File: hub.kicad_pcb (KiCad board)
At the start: 2 copper layers, 0 parts

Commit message: chore(revb): checkpoint current KiCad files before TI revision
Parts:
- added T1: 750313638, isolator-lib:WE_750313638, F.Cu at (166.2, 113.7)

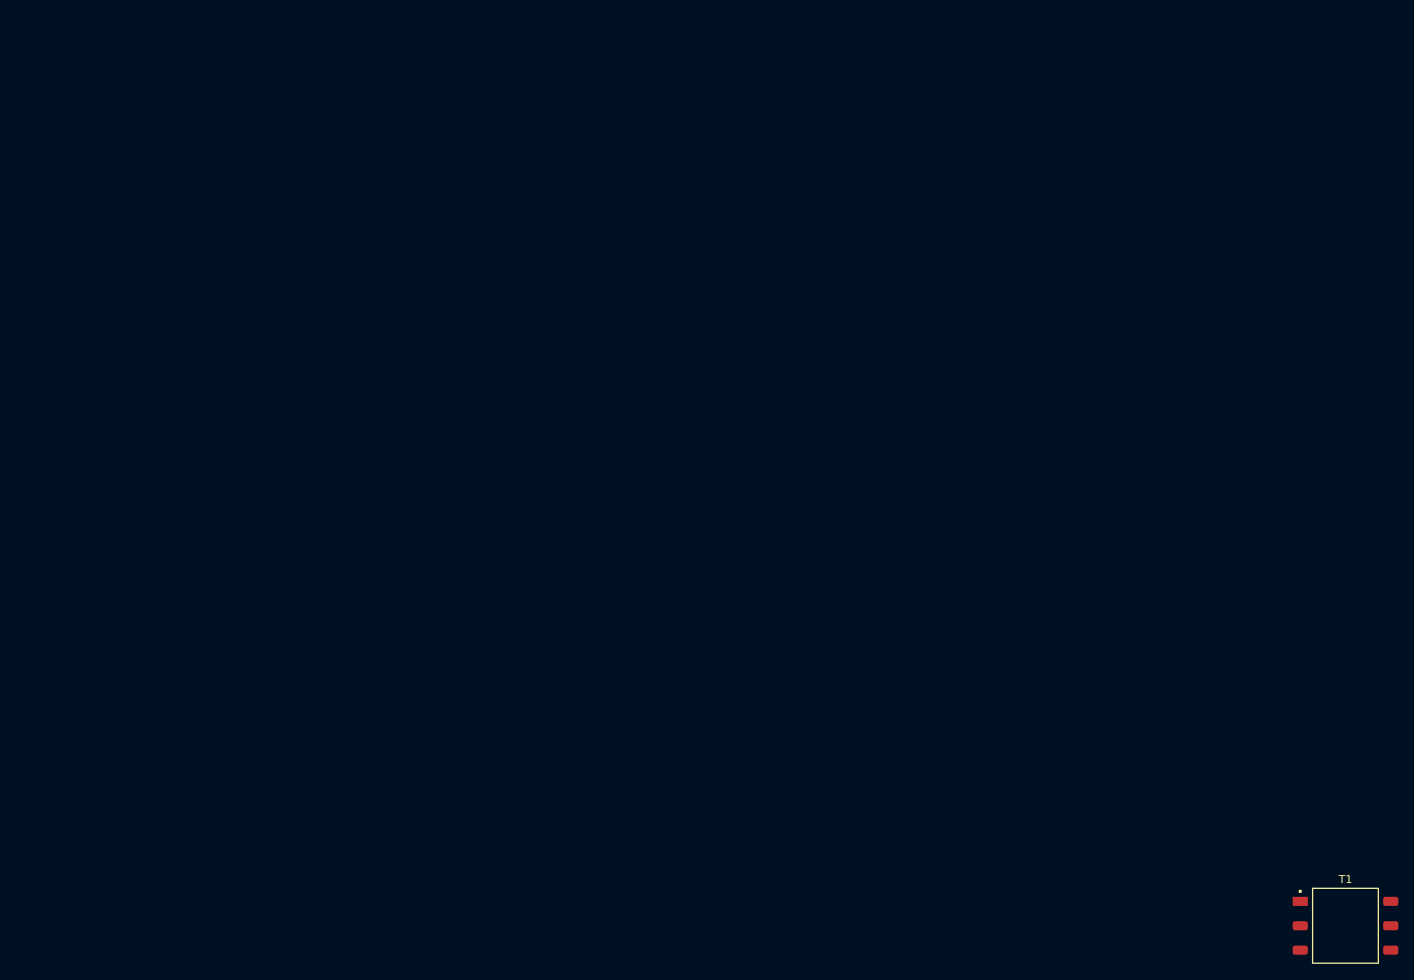
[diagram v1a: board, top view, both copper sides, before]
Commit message: feat(revc): place synchronized unrouted board and correct bus startup
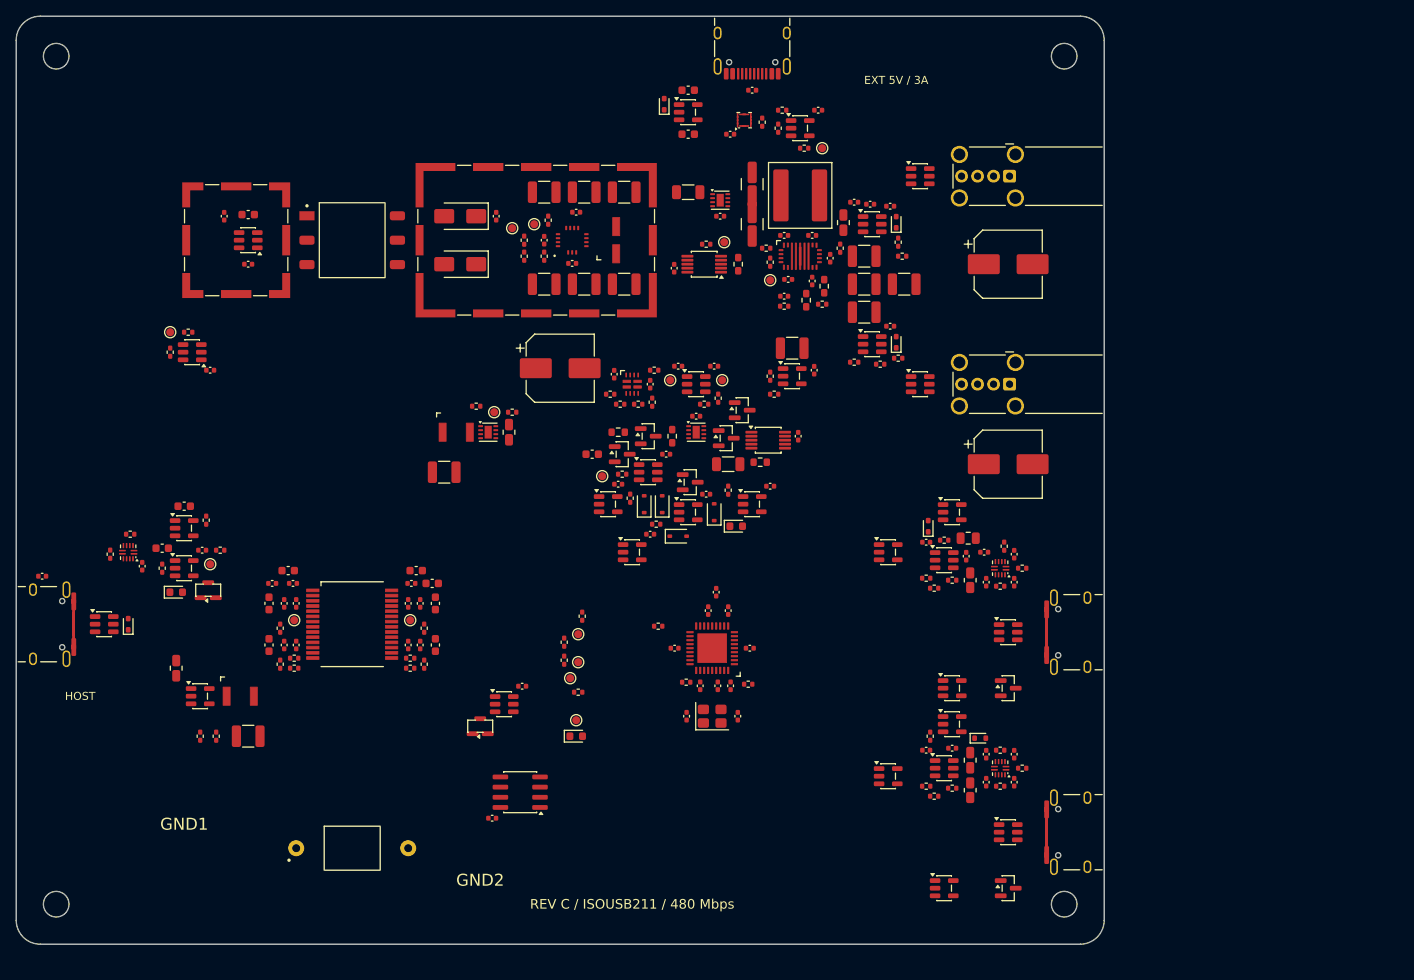
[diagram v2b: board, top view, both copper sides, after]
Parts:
- added C1: 100nF, hub-lib:C_0402_1005Metric, F.Cu at (3.25, 70.0)
- added C10: 100nF, hub-lib:C_0402_1005Metric, F.Cu at (26.0, 25.0)
- added C100: 100nF, hub-lib:C_0402_1005Metric, F.Cu at (121.2, 70.8)
- added C101: 100nF, hub-lib:C_0402_1005Metric, F.Cu at (124.8, 67.2)
- added C102: 100nF, hub-lib:C_0402_1005Metric, F.Cu at (124.8, 70.8)
- added C103: 100nF, hub-lib:C_0402_1005Metric, F.Cu at (121.2, 92.2)
- added C104: 100nF, hub-lib:C_0402_1005Metric, F.Cu at (121.2, 95.8)
- added C105: 100nF, hub-lib:C_0402_1005Metric, F.Cu at (124.8, 92.2)
- added C106: 100nF, hub-lib:C_0402_1005Metric, F.Cu at (124.8, 95.8)
- added C107: 100nF, hub-lib:C_0402_1005Metric, F.Cu at (86.2, 59.8)
- added C108: 100nF, hub-lib:C_0402_1005Metric, F.Cu at (75.2, 58.5)
- added C109: 100nF, hub-lib:C_0402_1005Metric, F.Cu at (79.2, 64.8)
- added C11: 4.7uF, hub-lib:C_0603_1608Metric, F.Cu at (29.0, 24.8)
- added C110: 100nF, hub-lib:C_0402_1005Metric, F.Cu at (82.2, 31.5)
- added C112: 100nF, hub-lib:C_0402_1005Metric, F.Cu at (97.8, 52.5)
- added C113: 4.7uF, hub-lib:C_0805_2012Metric, F.Cu at (20.0, 81.5)
- added C114: 22uF, hub-lib:C_1210_3225Metric, F.Cu at (29.0, 90.0)
- added C115: 22nF, hub-lib:C_0402_1005Metric, F.Cu at (85.0, 50.0)
- added C116: 22uF, hub-lib:C_1210_3225Metric, F.Cu at (97.0, 41.5)
- added C117: 100nF, hub-lib:C_0402_1005Metric, F.Cu at (99.8, 44.2)
- added C12: 100nF, hub-lib:C_0402_1005Metric, F.Cu at (29.0, 31.0)
- added C13: 22uF, hub-lib:C_1210_3225Metric, F.Cu at (66.0, 33.5)
- added C14: 100nF, hub-lib:C_0402_1005Metric, F.Cu at (60.0, 25.0)
- added C15: 22uF, hub-lib:C_1210_3225Metric, F.Cu at (71.0, 33.5)
- added C16: 22uF, hub-lib:C_1210_3225Metric, F.Cu at (76.0, 33.5)
- added C17: 100nF, hub-lib:C_0402_1005Metric, F.Cu at (69.5, 30.9)
- added C18: 22uF, hub-lib:C_1210_3225Metric, F.Cu at (66.0, 22.0)
- added C19: 22uF, hub-lib:C_1210_3225Metric, F.Cu at (71.0, 22.0)
- added C2: 1uF, hub-lib:C_0603_1608Metric, F.Cu at (21.0, 61.2)
- added C20: 22uF, hub-lib:C_1210_3225Metric, F.Cu at (76.0, 22.0)
- added C21: 100nF, hub-lib:C_0402_1005Metric, F.Cu at (70.0, 24.5)
- added C22: 100nF, hub-lib:C_0402_1005Metric, F.Cu at (66.0, 28.0)
- added C23: 100nF, hub-lib:C_0402_1005Metric, F.Cu at (92.0, 9.25)
- added C24: 1uF, hub-lib:C_0603_1608Metric, F.Cu at (84.0, 9.25)
- added C25: 100nF, hub-lib:C_0402_1005Metric, F.Cu at (89.2, 14.8)
- added C26: 100nF, hub-lib:C_0402_1005Metric, F.Cu at (100.2, 11.8)
- added C27: 100nF, hub-lib:C_0402_1005Metric, F.Cu at (74.8, 44.8)
- added C28: 1uF, hub-lib:C_0603_1608Metric, F.Cu at (50.0, 69.3)
- added C29: 100nF, hub-lib:C_0402_1005Metric, F.Cu at (49.4, 70.9)
- added C3: 1uF, hub-lib:C_0603_1608Metric, F.Cu at (34.0, 69.3)
- added C30: 10uF, hub-lib:C_0805_2012Metric, F.Cu at (61.6, 52.0)
- added C31: 22uF, hub-lib:C_1210_3225Metric, F.Cu at (53.5, 57.0)
- added C32: 27pF, hub-lib:C_0402_1005Metric, F.Cu at (83.8, 87.5)
- added C33: 27pF, hub-lib:C_0402_1005Metric, F.Cu at (90.2, 87.5)
- added C34: 100nF, hub-lib:C_0402_1005Metric, F.Cu at (87.5, 72.0)
- added C35: 100nF, hub-lib:C_0402_1005Metric, F.Cu at (91.7, 79.0)
- added C36: 100nF, hub-lib:C_0402_1005Metric, F.Cu at (89.0, 74.3)
- added C37: 100nF, hub-lib:C_0402_1005Metric, F.Cu at (86.5, 74.3)
- added C38: 100nF, hub-lib:C_0402_1005Metric, F.Cu at (82.3, 79.0)
- added C39: 100nF, hub-lib:C_0402_1005Metric, F.Cu at (85.5, 83.7)
- added C4: 100nF, hub-lib:C_0402_1005Metric, F.Cu at (34.6, 70.9)
- added C40: 100nF, hub-lib:C_0402_1005Metric, F.Cu at (89.3, 83.7)
- added C41: 4.7uF, hub-lib:C_0603_1608Metric, F.Cu at (72.0, 54.8)
- added C42: 100nF, hub-lib:C_0402_1005Metric, F.Cu at (63.2, 83.8)
- added C43: 100nF, hub-lib:C_0402_1005Metric, F.Cu at (104.8, 23.2)
- added C44: 220uF, hub-lib:CP_Elec_8x6.2, F.Cu at (124.0, 31.0)
- added C45: 100nF, hub-lib:C_0402_1005Metric, F.Cu at (109.2, 23.8)
- added C46: 100nF, hub-lib:C_0402_1005Metric, F.Cu at (106.8, 23.5)
- added C47: 220uF, hub-lib:CP_Elec_8x6.2, F.Cu at (124.0, 56.0)
- added C48: 100nF, hub-lib:C_0402_1005Metric, F.Cu at (109.2, 38.8)
- added C49: 100nF, hub-lib:C_0402_1005Metric, F.Cu at (113.8, 65.8)
- added C50: 10uF, hub-lib:C_0805_2012Metric, F.Cu at (119.0, 65.2)
- added C51: 100nF, hub-lib:C_0402_1005Metric, F.Cu at (118.8, 67.5)
- added C55: 100nF, hub-lib:C_0402_1005Metric, F.Cu at (113.8, 91.8)
- added C56: 10uF, hub-lib:C_0805_2012Metric, F.Cu at (119.2, 93.0)
- added C57: 100nF, hub-lib:C_0402_1005Metric, F.Cu at (117.0, 91.5)
- added C59: 100nF, hub-lib:C_0402_1005Metric, F.Cu at (87.7, 83.7)
- added C61: 1uF, hub-lib:C_0603_1608Metric, F.Cu at (18.2, 66.5)
- added C62: 100nF, hub-lib:C_0402_1005Metric, F.Cu at (24.2, 44.2)
- added C63: 100nF, hub-lib:C_0402_1005Metric, F.Cu at (32.0, 70.9)
- added C64: 1uF, hub-lib:C_0603_1608Metric, F.Cu at (52.0, 70.9)
- added C65: 4.7uF, hub-lib:C_0603_1608Metric, F.Cu at (31.6, 73.4)
- added C66: 100nF, hub-lib:C_0402_1005Metric, F.Cu at (33.5, 73.4)
- added C67: 10nF, hub-lib:C_0402_1005Metric, F.Cu at (35.0, 73.4)
- added C68: 4.7uF, hub-lib:C_0603_1608Metric, F.Cu at (31.6, 78.6)
- added C69: 100nF, hub-lib:C_0402_1005Metric, F.Cu at (33.5, 78.6)
- added C7: 100nF, hub-lib:C_0402_1005Metric, F.Cu at (15.8, 68.8)
- added C70: 10nF, hub-lib:C_0402_1005Metric, F.Cu at (35.0, 78.6)
- added C71: 4.7uF, hub-lib:C_0603_1608Metric, F.Cu at (52.4, 73.4)
- added C72: 100nF, hub-lib:C_0402_1005Metric, F.Cu at (50.5, 73.4)
- added C73: 10nF, hub-lib:C_0402_1005Metric, F.Cu at (49.0, 73.4)
- added C74: 4.7uF, hub-lib:C_0603_1608Metric, F.Cu at (52.4, 78.6)
- added C75: 100nF, hub-lib:C_0402_1005Metric, F.Cu at (50.5, 78.6)
- added C76: 10nF, hub-lib:C_0402_1005Metric, F.Cu at (49.0, 78.6)
- added C77: 1uF, hub-lib:C_0603_1608Metric, F.Cu at (84.0, 14.8)
- added C78: 10nF, hub-lib:C_0402_1005Metric, F.Cu at (88.0, 25.0)
- added C79: 22uF, hub-lib:C_1210_3225Metric, F.Cu at (92.0, 21.0)
- added C8: 100nF, hub-lib:C_0402_1005Metric, F.Cu at (23.2, 66.8)
- added C80: 22uF, hub-lib:C_1210_3225Metric, F.Cu at (92.0, 26.0)
- added C81: 100nF, hub-lib:C_0402_1005Metric, F.Cu at (96.5, 32.9)
- added C82: 100nF, hub-lib:C_0402_1005Metric, F.Cu at (96.0, 27.4)
- added C83: 100nF, hub-lib:C_0402_1005Metric, F.Cu at (99.5, 27.4)
- added C84: 10uF, hub-lib:C_0805_2012Metric, F.Cu at (103.4, 25.8)
- added C85: 22uF, hub-lib:C_1210_3225Metric, F.Cu at (106.0, 30.0)
- added C86: 22uF, hub-lib:C_1210_3225Metric, F.Cu at (106.0, 33.5)
- added C87: 22uF, hub-lib:C_1210_3225Metric, F.Cu at (106.0, 37.0)
- added C88: 22uF, hub-lib:C_1210_3225Metric, F.Cu at (111.0, 33.5)
- added C89: 100nF, hub-lib:C_0402_1005Metric, F.Cu at (99.5, 33.1)
- added C90: 220nF, hub-lib:C_0402_1005Metric, F.Cu at (96.0, 35.0)
- added C91: 100pF, hub-lib:C_0402_1005Metric, F.Cu at (101.8, 30.2)
- added C92: 220uF, hub-lib:CP_Elec_8x6.2, F.Cu at (68.0, 44.0)
- added C93: 100nF, hub-lib:C_0402_1005Metric, F.Cu at (79.2, 46.0)
- added C94: 100nF, hub-lib:C_0402_1005Metric, F.Cu at (81.2, 54.8)
- added C95: 100nF, hub-lib:C_0402_1005Metric, F.Cu at (94.2, 58.8)
- added C96: 100nF, hub-lib:C_0402_1005Metric, F.Cu at (82.8, 43.8)
- added C97: 100nF, hub-lib:C_0402_1005Metric, F.Cu at (87.2, 43.8)
- added C98: 100nF, hub-lib:C_0402_1005Metric, F.Cu at (59.5, 100.2)
- added C99: 100nF, hub-lib:C_0402_1005Metric, F.Cu at (121.0, 67.0)
- added CY1: 1nF Y1, hub-lib:C_Disc_D7.0mm_W5.5mm_P14.00mm, F.Cu at (35.0, 104.0)
- added D1: T6V0S5A-7, hub-lib:D_SOD-523, F.Cu at (14.0, 76.0)
- added D10: T6V0S5A-7, hub-lib:D_SOD-523, F.Cu at (114.0, 63.8)
- added D13: T6V0S5A-7, hub-lib:D_SOD-523, F.Cu at (120.5, 90.2)
- added D14: BAT54WS, hub-lib:D_SOD-323, F.Cu at (80.8, 61.0)
- added D15: BAT54WS, hub-lib:D_SOD-323, F.Cu at (82.8, 65.0)
- added D16: BAT54WS, hub-lib:D_SOD-323, F.Cu at (87.2, 62.0)
- added D17: BAT54WS, hub-lib:D_SOD-323, F.Cu at (78.5, 61.0)
- added D2: GREEN, hub-lib:LED_0603_1608Metric, F.Cu at (20.0, 72.0)
- added D20: BAT54C, hub-lib:SOT-23, F.Cu at (84.2, 58.2)
- added D21: BAT54C, hub-lib:SOT-23, F.Cu at (90.8, 49.2)
- added D22: BAT54C, hub-lib:SOT-23, F.Cu at (75.8, 54.8)
- added D23: BAT54C, hub-lib:SOT-23, F.Cu at (79.0, 52.5)
- added D3: SS34, hub-lib:D_SMA, F.Cu at (55.5, 31.0)
- added D4: SS34, hub-lib:D_SMA, F.Cu at (55.5, 25.0)
- added D5: T6V0S5A-7, hub-lib:D_SOD-523, F.Cu at (81.0, 11.0)
- added D6: GREEN, hub-lib:LED_0603_1608Metric, F.Cu at (90.0, 63.8)
- added D7: GREEN, hub-lib:LED_0603_1608Metric, F.Cu at (70.0, 90.0)
- added D8: T6V0S5A-7, hub-lib:D_SOD-523, F.Cu at (110.0, 25.8)
- added D9: T6V0S5A-7, hub-lib:D_SOD-523, F.Cu at (110.0, 40.8)
- added H1: M3 NPTH, hub-lib:MountingHole_3.2mm_M3, F.Cu at (5.00, 5.00)
- added H2: M3 NPTH, hub-lib:MountingHole_3.2mm_M3, F.Cu at (131.0, 5.00)
- added H3: M3 NPTH, hub-lib:MountingHole_3.2mm_M3, F.Cu at (5.00, 111.0)
- added H4: M3 NPTH, hub-lib:MountingHole_3.2mm_M3, F.Cu at (131.0, 111.0)
- added J1: USB-C USB2.0, hub-lib:USB_C_Receptacle_HRO_TYPE-C-31-M-12, F.Cu at (3.15, 76.0)
- added J2: USB-C 5V POWER, hub-lib:USB_C_Receptacle_HRO_TYPE-C-31-M-12, F.Cu at (92.0, 3.15)
- added J3: USB-A, hub-lib:USB_A_Wuerth_614004134726_Horizontal, F.Cu at (124.2, 20.0)
- added J4: USB-A, hub-lib:USB_A_Wuerth_614004134726_Horizontal, F.Cu at (124.2, 46.0)
- added J5: USB-C USB2.0, hub-lib:USB_C_Receptacle_HRO_TYPE-C-31-M-12, F.Cu at (132.8, 77.0)
- added J6: USB-C USB2.0, hub-lib:USB_C_Receptacle_HRO_TYPE-C-31-M-12, F.Cu at (132.8, 102.0)
- added L1: 1.5uH, hub-lib:Coilcraft_XFL4020_4x4mm, F.Cu at (75.0, 28.0)
- added L2: 2.2uH, hub-lib:Coilcraft_XFL4020_4x4mm, F.Cu at (55.0, 52.0)
- added L3: 4.7uH, hub-lib:L_Coilcraft_XAL7070-XXX, F.Cu at (98.0, 22.4)
- added L4: 2.2uH, hub-lib:Coilcraft_XFL4020_4x4mm, F.Cu at (28.0, 85.0)
- added Q2: 2N7002, hub-lib:SOT-23, F.Cu at (24.0, 71.8)
- added Q3: 2N7002, hub-lib:SOT-23, F.Cu at (88.8, 52.8)
- added Q4: 2N7002, hub-lib:SOT-23, F.Cu at (58.0, 88.8)
- added Q5: 2N7002, hub-lib:SOT-23, F.Cu at (124.0, 84.0)
- added Q6: 2N7002, hub-lib:SOT-23, F.Cu at (124.0, 109.0)
- added R1: 909kR, hub-lib:R_0402_1005Metric, F.Cu at (14.2, 64.8)
- added R10: 0R, hub-lib:R_0402_1005Metric, F.Cu at (66.5, 25.5)
- added R101: 100kR, hub-lib:R_0402_1005Metric, F.Cu at (103.0, 29.0)
- added R102: 100kR, hub-lib:R_0402_1005Metric, F.Cu at (104.8, 43.2)
- added R103: 100kR, hub-lib:R_0402_1005Metric, F.Cu at (113.8, 70.2)
- added R104: 100kR, hub-lib:R_0402_1005Metric, F.Cu at (113.8, 96.2)
- added R11: 100kR, hub-lib:R_0402_1005Metric, F.Cu at (66.0, 30.0)
- added R110: 20mR, hub-lib:R_1206_3216Metric, F.Cu at (84.0, 22.0)
- added R111: 2.87kR, hub-lib:R_0603_1608Metric, F.Cu at (90.2, 31.0)
- added R112: 0R, hub-lib:R_0402_1005Metric, F.Cu at (86.2, 28.5)
- added R114: 200kR, hub-lib:R_0402_1005Metric, F.Cu at (25.0, 90.0)
- added R115: 100kR, hub-lib:R_0402_1005Metric, F.Cu at (23.0, 90.0)
- added R116: 10mR, hub-lib:R_1206_3216Metric, F.Cu at (89.0, 56.0)
- added R117: 1.1kR, hub-lib:R_0603_1608Metric, F.Cu at (93.0, 55.8)
- added R119: 10kR, hub-lib:R_0402_1005Metric, F.Cu at (116.0, 65.5)
- added R12: 100kR, hub-lib:R_0402_1005Metric, F.Cu at (63.5, 28.0)
- added R120: 10kR, hub-lib:R_0402_1005Metric, F.Cu at (114.2, 90.0)
- added R121: 47kR, hub-lib:R_0402_1005Metric, F.Cu at (94.2, 45.0)
- added R122: 1kR, hub-lib:R_0402_1005Metric, F.Cu at (94.8, 47.2)
- added R15: 0R, hub-lib:R_0402_1005Metric, F.Cu at (63.5, 30.0)
- added R16: 909kR, hub-lib:R_0402_1005Metric, F.Cu at (93.2, 13.2)
- added R17: 10kR, hub-lib:R_0402_1005Metric, F.Cu at (95.8, 11.8)
- added R18: 10kR, hub-lib:R_0402_1005Metric, F.Cu at (95.2, 14.0)
- added R19: 100kR, hub-lib:R_0402_1005Metric, F.Cu at (98.5, 16.5)
- added R2: 10kR, hub-lib:R_0402_1005Metric, F.Cu at (18.2, 69.0)
- added R20: 10kR, hub-lib:R_0603_1608Metric, F.Cu at (101.0, 33.8)
- added R21: 3kR, hub-lib:R_0603_1608Metric, F.Cu at (98.8, 35.5)
- added R22: 0R, hub-lib:R_0402_1005Metric, F.Cu at (96.0, 36.2)
- added R23: 17.8kR, hub-lib:R_0402_1005Metric, F.Cu at (77.8, 48.5)
- added R24: 10kR, hub-lib:R_0402_1005Metric, F.Cu at (79.5, 48.2)
- added R25: 23.7kR, hub-lib:R_0402_1005Metric, F.Cu at (75.5, 48.5)
- added R26: 10.2kR, hub-lib:R_0402_1005Metric, F.Cu at (74.2, 47.2)
- added R27: 29.8kR, hub-lib:R_0402_1005Metric, F.Cu at (79.8, 44.2)
- added R28: 10kR, hub-lib:R_0402_1005Metric, F.Cu at (89.0, 59.2)
- added R29: 3.3kR, hub-lib:R_0402_1005Metric, F.Cu at (75.8, 57.2)
- added R3: 10kR, hub-lib:R_0402_1005Metric, F.Cu at (11.8, 67.2)
- added R30: 3.3kR, hub-lib:R_0402_1005Metric, F.Cu at (62.0, 49.5)
- added R31: 100kR, hub-lib:R_0402_1005Metric, F.Cu at (83.8, 83.2)
- added R32: 12kR, hub-lib:R_0402_1005Metric, F.Cu at (91.5, 83.5)
- added R33: 10kR, hub-lib:R_0402_1005Metric, F.Cu at (68.5, 80.5)
- added R34: 4.7kR, hub-lib:R_0402_1005Metric, F.Cu at (68.5, 78.2)
- added R35: 10kR, hub-lib:R_0402_1005Metric, F.Cu at (80.2, 76.2)
- added R36: 4.7kR, hub-lib:R_0402_1005Metric, F.Cu at (70.8, 75.0)
- added R37: 1kR, hub-lib:R_0402_1005Metric, F.Cu at (70.2, 84.5)
- added R38: 46.4kR, hub-lib:R_0402_1005Metric, F.Cu at (110.2, 28.2)
- added R39: 46.4kR, hub-lib:R_0402_1005Metric, F.Cu at (110.2, 42.8)
- added R4: 100kR, hub-lib:R_0402_1005Metric, F.Cu at (25.5, 66.8)
- added R40: 46.4kR, hub-lib:R_0402_1005Metric, F.Cu at (117.0, 70.5)
- added R44: 46.4kR, hub-lib:R_0402_1005Metric, F.Cu at (117.0, 96.5)
- added R47: 100kR, hub-lib:R_0402_1005Metric, F.Cu at (110.8, 30.0)
- added R48: 100kR, hub-lib:R_0402_1005Metric, F.Cu at (108.0, 43.5)
- added R49: 100kR, hub-lib:R_0402_1005Metric, F.Cu at (114.8, 71.5)
- added R5: 28.7kR, hub-lib:R_0402_1005Metric, F.Cu at (19.2, 42.0)
- added R50: 100kR, hub-lib:R_0402_1005Metric, F.Cu at (114.8, 97.5)
- added R51: 0R, hub-lib:R_0402_1005Metric, F.Cu at (34.8, 80.2)
- added R52: 0R, hub-lib:R_0402_1005Metric, F.Cu at (33.0, 76.5)
- added R53: 0R, hub-lib:R_0402_1005Metric, F.Cu at (34.8, 81.5)
- added R54: 0R, hub-lib:R_0402_1005Metric, F.Cu at (33.0, 81.0)
- added R55: 0R, hub-lib:R_0402_1005Metric, F.Cu at (49.2, 80.2)
- added R56: 0R, hub-lib:R_0402_1005Metric, F.Cu at (51.0, 76.5)
- added R57: 0R, hub-lib:R_0402_1005Metric, F.Cu at (49.2, 81.5)
- added R58: 0R, hub-lib:R_0402_1005Metric, F.Cu at (51.0, 81.0)
- added R59: 49.9kR, hub-lib:R_0402_1005Metric, F.Cu at (94.2, 30.8)
- added R6: 10kR, hub-lib:R_0402_1005Metric, F.Cu at (21.5, 39.5)
- added R60: 2.7kR, hub-lib:R_0402_1005Metric, F.Cu at (100.8, 36.0)
- added R61: 10kR, hub-lib:R_0402_1005Metric, F.Cu at (93.8, 29.0)
- added R62: 75kR, hub-lib:R_0402_1005Metric, F.Cu at (87.8, 47.8)
- added R63: 10kR, hub-lib:R_0402_1005Metric, F.Cu at (86.0, 48.5)
- added R64: 100kR, hub-lib:R_0603_1608Metric, F.Cu at (82.0, 52.5)
- added R65: 10kR, hub-lib:R_0603_1608Metric, F.Cu at (75.2, 52.0)
- added R66: 10kR, hub-lib:R_0402_1005Metric, F.Cu at (76.8, 60.2)
- added R67: 10kR, hub-lib:R_0402_1005Metric, F.Cu at (57.5, 48.8)
- added R72: 4.7kR, hub-lib:R_0402_1005Metric, F.Cu at (123.5, 66.2)
- added R73: 10kR, hub-lib:R_0402_1005Metric, F.Cu at (123.0, 71.2)
- added R74: 909kR, hub-lib:R_0402_1005Metric, F.Cu at (125.8, 69.0)
- added R75: 4.7kR, hub-lib:R_0402_1005Metric, F.Cu at (123.0, 91.8)
- added R76: 10kR, hub-lib:R_0402_1005Metric, F.Cu at (123.0, 96.2)
- added R77: 909kR, hub-lib:R_0402_1005Metric, F.Cu at (125.8, 94.0)
- added R81: 100R, hub-lib:R_0805_2012Metric, F.Cu at (119.2, 70.5)
- added R82: 100R, hub-lib:R_0805_2012Metric, F.Cu at (119.2, 96.8)
- added R83: 10kR, hub-lib:R_0402_1005Metric, F.Cu at (80.0, 63.5)
- added R9: 3.3kR, hub-lib:R_0402_1005Metric, F.Cu at (23.8, 63.0)
- added SH1: BMI-S-201-F, hub-lib:Laird_Technologies_BMI-S-201-F_13.66x12.70mm, F.Cu at (27.5, 28.0)
- added SH2: BMI-S-209-F, hub-lib:Laird_Technologies_BMI-S-209-F_29.36x18.50mm, F.Cu at (65.0, 28.0)
- added TP1: HOST_PWR_OK, hub-lib:TestPoint_Pad_D1.0mm, F.Cu at (24.2, 68.5)
- added TP10: PORT_SUPPLY, hub-lib:TestPoint_Pad_D1.0mm, F.Cu at (88.2, 45.5)
- added TP11: PORT_RAIL_OK, hub-lib:TestPoint_Pad_D1.0mm, F.Cu at (73.2, 57.5)
- added TP12: ISO_3V3, hub-lib:TestPoint_Pad_D1.0mm, F.Cu at (59.8, 49.5)
- added TP13: HUB_RESET_N, hub-lib:TestPoint_Pad_D1.0mm, F.Cu at (70.2, 80.8)
- added TP14: HUB_SDA, hub-lib:TestPoint_Pad_D1.0mm, F.Cu at (70.2, 77.2)
- added TP15: HUB_SCL, hub-lib:TestPoint_Pad_D1.0mm, F.Cu at (69.2, 82.8)
- added TP16: GND2, hub-lib:TestPoint_Pad_D1.0mm, F.Cu at (70.0, 88.0)
- added TP17: EXT_CURRENT_OK, hub-lib:TestPoint_Pad_D1.0mm, F.Cu at (88.5, 28.2)
- added TP2: HOST_LIMIT_N, hub-lib:TestPoint_Pad_D1.0mm, F.Cu at (19.2, 39.5)
- added TP3: ISO_SIDE_OK, hub-lib:TestPoint_Pad_D1.0mm, F.Cu at (34.8, 75.5)
- added TP4: HOST_PRESENT, hub-lib:TestPoint_Pad_D1.0mm, F.Cu at (49.2, 75.5)
- added TP5: DCDC_RAW, hub-lib:TestPoint_Pad_D1.0mm, F.Cu at (64.8, 26.0)
- added TP6: ISO_5V_PRE, hub-lib:TestPoint_Pad_D1.0mm, F.Cu at (62.0, 26.5)
- added TP7: EXT_3A_OK, hub-lib:TestPoint_Pad_D1.0mm, F.Cu at (100.8, 16.5)
- added TP8: EXT_REG_5V, hub-lib:TestPoint_Pad_D1.0mm, F.Cu at (94.2, 33.0)
- added TP9: ISO_5V, hub-lib:TestPoint_Pad_D1.0mm, F.Cu at (81.8, 45.5)
- added U1: ISOUSB211DPR, hub-lib:TI_DP0028A-C02_HV_SSOP28_8.2mm_Clearance, F.Cu at (42.0, 76.0)
- added U10: TPS62162DSGR, hub-lib:Texas_DSG0008A_WSON-8-1EP_2x2mm_P0.5mm_EP0.9x1.6mm, F.Cu at (59.0, 52.0)
- added U11: USB2514B-I/M2, hub-lib:Microchip_SQFN36_6x6mm_EP3.7mm, F.Cu at (87.0, 79.0)
- added U12: TPS2553DBVR, hub-lib:SOT-23-6, F.Cu at (107.0, 26.0)
- added U13: TPS2553DBVR, hub-lib:SOT-23-6, F.Cu at (107.0, 41.0)
- added U14: TPS2553DBVR, hub-lib:SOT-23-6, F.Cu at (116.0, 68.0)
- added U15: TPS2553DBVR, hub-lib:SOT-23-6, F.Cu at (116.0, 94.0)
- added U16: USBLC6-2SC6, hub-lib:SOT-23-6, F.Cu at (113.0, 20.0)
- added U17: USBLC6-2SC6, hub-lib:SOT-23-6, F.Cu at (113.0, 46.0)
- added U18: USBLC6-2SC6, hub-lib:SOT-23-6, F.Cu at (124.0, 77.0)
- added U19: USBLC6-2SC6, hub-lib:SOT-23-6, F.Cu at (124.0, 102.0)
- added U2: USBLC6-2SC6, hub-lib:SOT-23-6, F.Cu at (11.0, 76.0)
- added U20: TUSB320LAIRWBR, hub-lib:Texas_X2QFN-12_1.6x1.6mm_P0.4mm, F.Cu at (123.0, 69.0)
- added U21: TUSB320LAIRWBR, hub-lib:Texas_X2QFN-12_1.6x1.6mm_P0.4mm, F.Cu at (123.0, 94.0)
- added U22: TLV75533PDBVR, hub-lib:SOT-23-5, F.Cu at (21.0, 64.0)
- added U23: TLV75533PDBVR, hub-lib:SOT-23-5, F.Cu at (84.0, 12.0)
- added U24: SN74LVC1G04DBVR, hub-lib:SOT-23-5, F.Cu at (21.0, 69.0)
- added U25: SN74LVC1G02DBVR, hub-lib:SOT-23-5, F.Cu at (98.0, 14.0)
- added U26: TPS2553DBVR, hub-lib:SOT-23-6, F.Cu at (22.0, 42.0)
- added U27: TPS22975DSGR, hub-lib:Texas_DSG0008A_WSON-8-1EP_2x2mm_P0.5mm_EP0.9x1.6mm, F.Cu at (88.0, 23.0)
- added U28: TPS552892RYQR, hub-lib:TI_RYQ0021A_VQFN21_3x5mm, F.Cu at (98.0, 30.0)
- added U29: TPS2553DBVR, hub-lib:SOT-23-6, F.Cu at (85.0, 46.0)
- added U3: TUSB320LAIRWBR, hub-lib:Texas_X2QFN-12_1.6x1.6mm_P0.4mm, F.Cu at (14.0, 67.0)
- added U30: TPS22975NDSGR, hub-lib:Texas_DSG0008A_WSON-8-1EP_2x2mm_P0.5mm_EP0.9x1.6mm, F.Cu at (85.0, 52.0)
- added U31: TPS3808G01DBVR, hub-lib:SOT-23-6, F.Cu at (79.0, 57.0)
- added U32: SN74LVC1G08DBVR, hub-lib:SOT-23-5, F.Cu at (92.0, 61.0)
- added U33: TPS3808G33DBVR, hub-lib:SOT-23-6, F.Cu at (61.0, 86.0)
- added U34: 24LC02B-I/SN, hub-lib:SOIC-8_3.9x4.9mm_P1.27mm, F.Cu at (63.0, 97.0)
- added U35: SN74LVC1G04DBVR, hub-lib:SOT-23-5, F.Cu at (117.0, 62.0)
- added U36: SN74LVC1G04DBVR, hub-lib:SOT-23-5, F.Cu at (117.0, 88.5)
- added U37: SN74LVC1G08DBVR, hub-lib:SOT-23-5, F.Cu at (109.0, 67.0)
- added U38: SN74LVC1G08DBVR, hub-lib:SOT-23-5, F.Cu at (109.0, 95.0)
- added U39: SN74LVC1G04DBVR, hub-lib:SOT-23-5, F.Cu at (117.0, 84.0)
- added U40: SN74LVC1G04DBVR, hub-lib:SOT-23-5, F.Cu at (116.0, 109.0)
- added U41: SN74LVC1G08DBVR, hub-lib:SOT-23-5, F.Cu at (84.0, 62.0)
- added U42: SN74LVC1G04DBVR, hub-lib:SOT-23-5, F.Cu at (74.0, 61.0)
- added U43: SN74LVC1G08DBVR, hub-lib:SOT-23-5, F.Cu at (77.0, 67.0)
- added U45: TLV62568DBVR, hub-lib:SOT-23-5, F.Cu at (23.0, 85.0)
- added U46: INA300AIDGSR, hub-lib:MSOP-10_3x3mm_P0.5mm, F.Cu at (86.0, 31.0)
- added U47: INA300AIDGSR, hub-lib:MSOP-10_3x3mm_P0.5mm, F.Cu at (94.0, 53.0)
- added U48: SN74LVC1G17DBVR, hub-lib:SOT-23-5, F.Cu at (97.0, 45.0)
- added U5: SN6505BDBVR, hub-lib:SOT-23-6, F.Cu at (29.0, 28.0)
- added U6: TPS630701RNMR, hub-lib:TPS630701RNM_VQFN-HR-15, F.Cu at (69.5, 28.0)
- added U7: TUSB320LAIRWBR, hub-lib:Texas_X2QFN-12_1.6x1.6mm_P0.4mm, F.Cu at (91.0, 13.0)
- added U8: TPS2121RUXR, hub-lib:TI_RUX0012A_VQFN-HR12_2x2.5mm, F.Cu at (77.0, 46.0)
- added Y2: 24MHz, hub-lib:Crystal_SMD_3225-4Pin_3.2x2.5mm, F.Cu at (87.0, 87.5)
- T1: footprint isolator-lib:WE_750313638 -> hub-lib:WE_750313638
- moved T1 150.9 mm to (42.0, 28.0)
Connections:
- T1 pad 1: Net-(T1-N1) -> PRI_A
- T1 pad 2: VBUS_HOST -> HOST_CONVERTER_5V
- T1 pad 3: Net-(T1-N2) -> PRI_B
- T1 pad 4: Net-(D4-A) -> SEC_B
- T1 pad 6: Net-(D3-A) -> SEC_A
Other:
- board outline added: 136 x 116 mm
- copper layers 2 -> 4
- rule pad_to_mask_clearance: 0.05 -> 0
- board text added: "EXT 5V / 3A"
- board text added: "GND1"
- board text added: "GND2"
- board text added: "HOST"
- board text added: "JLC04161H-3313 / 4 LAYERS / 90 OHM USB TARGET"
- board text added: "REV C / ISOUSB211 / 480 Mbps"
- board text added: "UNROUTED — ALEX ROUTES ALL NETS"

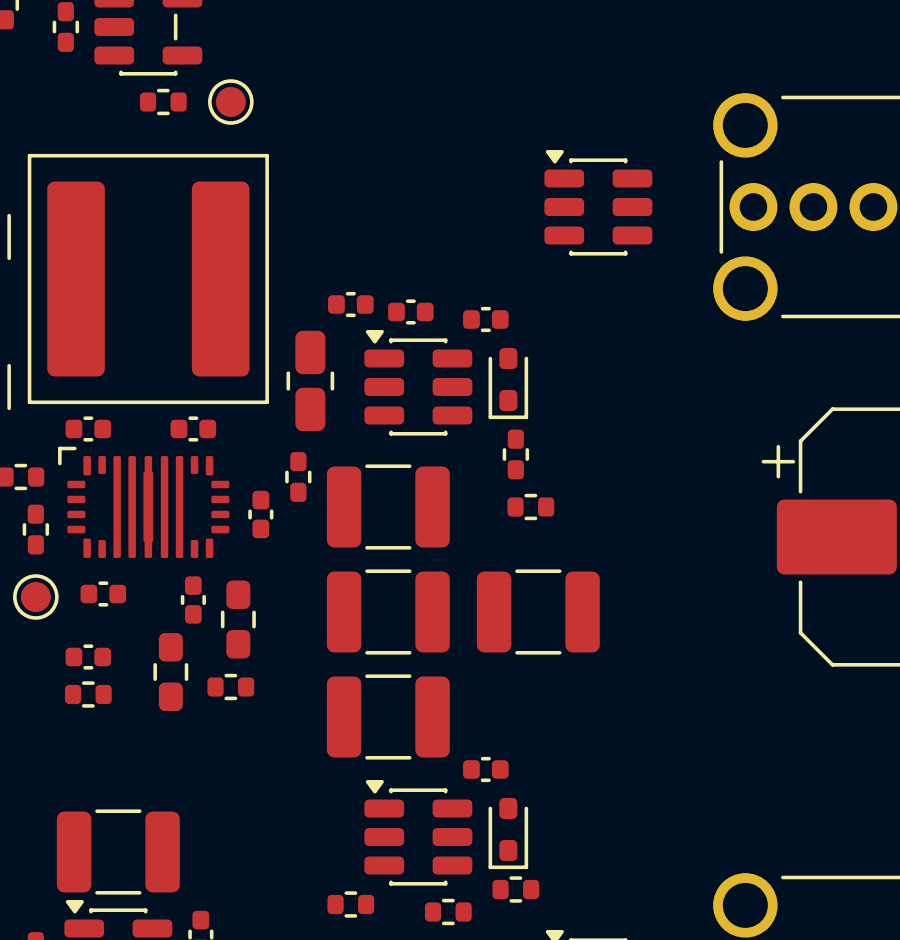
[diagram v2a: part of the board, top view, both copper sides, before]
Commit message: feat(revc): finish verified TI hub routing handoff
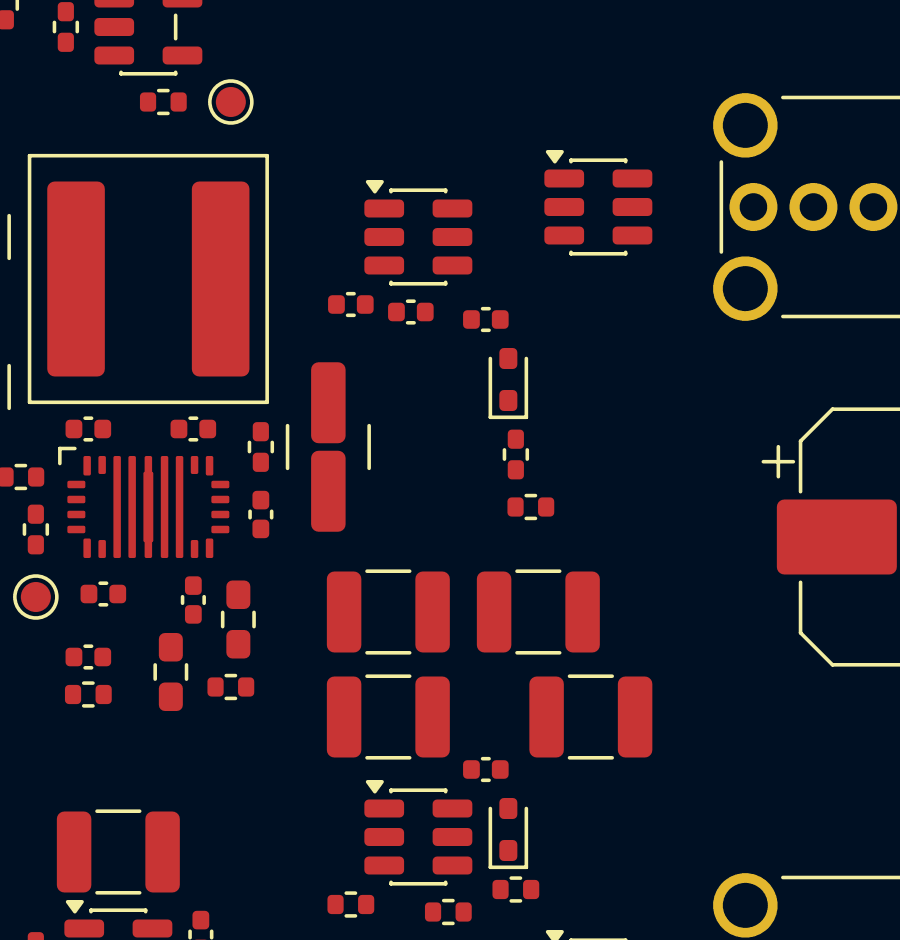
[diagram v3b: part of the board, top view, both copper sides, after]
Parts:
- C84: value 10uF -> 22uF; footprint hub-lib:C_0805_2012Metric -> hub-lib:C_1210_3225Metric
- R121: value 47kR -> 68kR
- moved C85 9.72 mm to (112.8, 37.0)
- moved U12 5.00 mm to (107.0, 21.0)
- moved C84 2.28 mm to (104.0, 28.0), turned to 270 degrees
- moved R101 1.60 mm to (101.8, 28.0)
